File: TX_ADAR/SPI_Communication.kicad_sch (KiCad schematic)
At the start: 16 parts, among them SW1 SW_SPDT, SW3 SW_SPDT, U10 TXB0101DBV, U11 TXB0101DBV, U14 TXB0101DBV, U19 TXB0101DBV

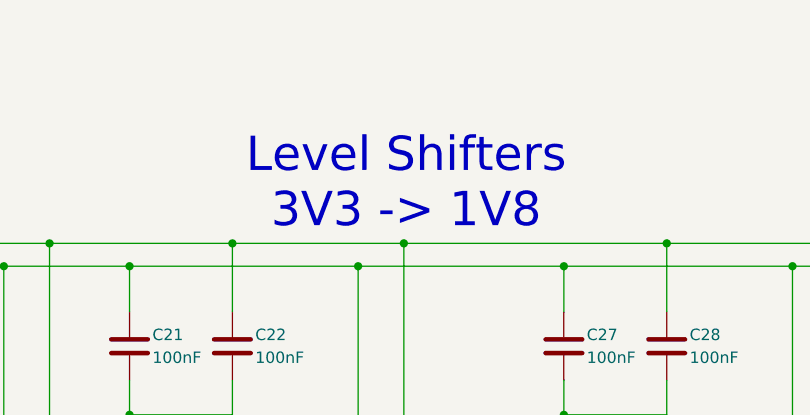
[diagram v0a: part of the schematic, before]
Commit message: Fixed tracks & added images to schem
NEED: Find 50 ohm impedance width for OSH Park
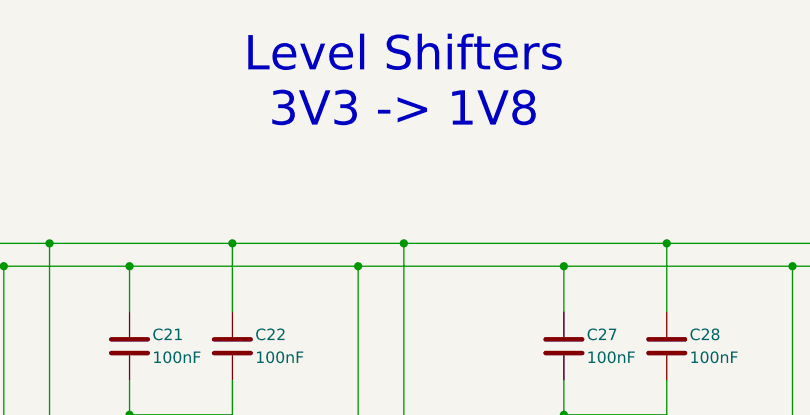
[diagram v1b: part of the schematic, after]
